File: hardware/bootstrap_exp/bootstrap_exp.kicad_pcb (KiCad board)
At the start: 4 copper layers, 45.7 x 35.6 mm, 32 parts, among them J1 Conn_Coaxial, J2 Conn_Coaxial, U1 OPA810, U2 OPA810, U3 OPA810, U4 OPA810

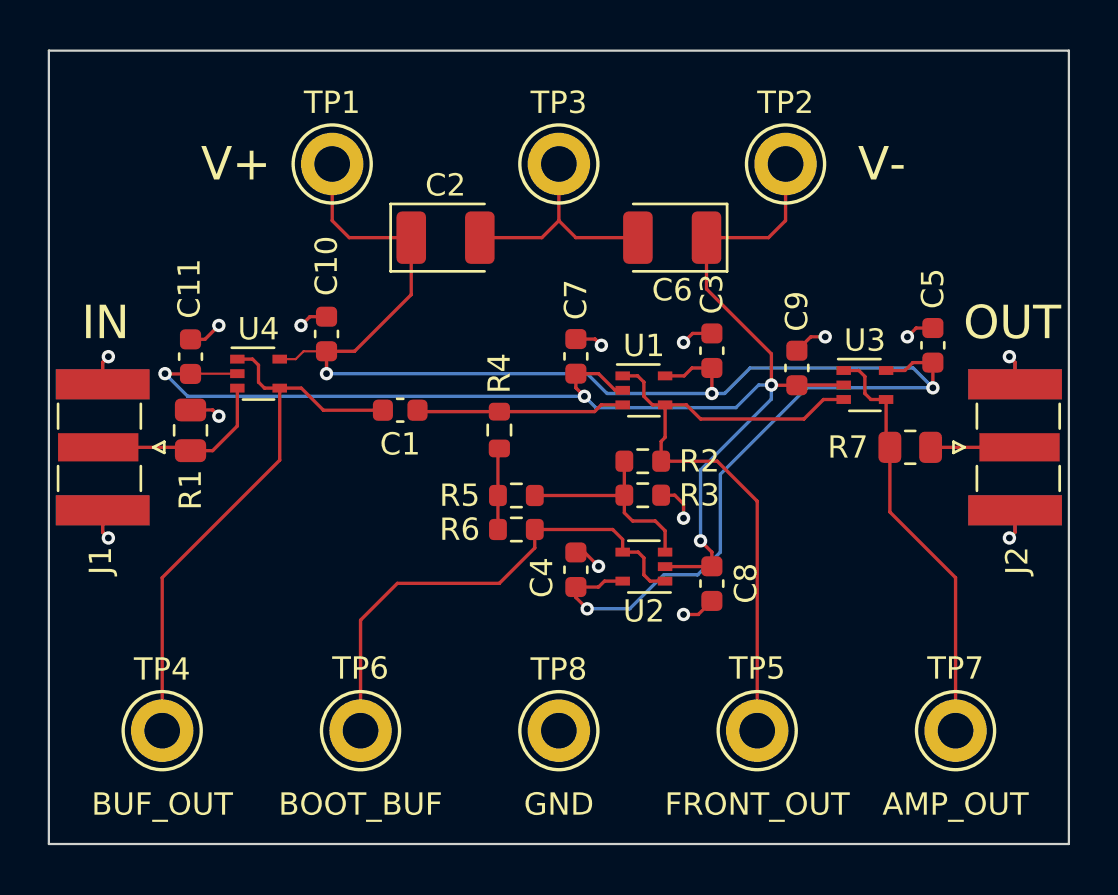
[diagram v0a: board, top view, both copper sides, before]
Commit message: Make edge cut extents an integer for width and height
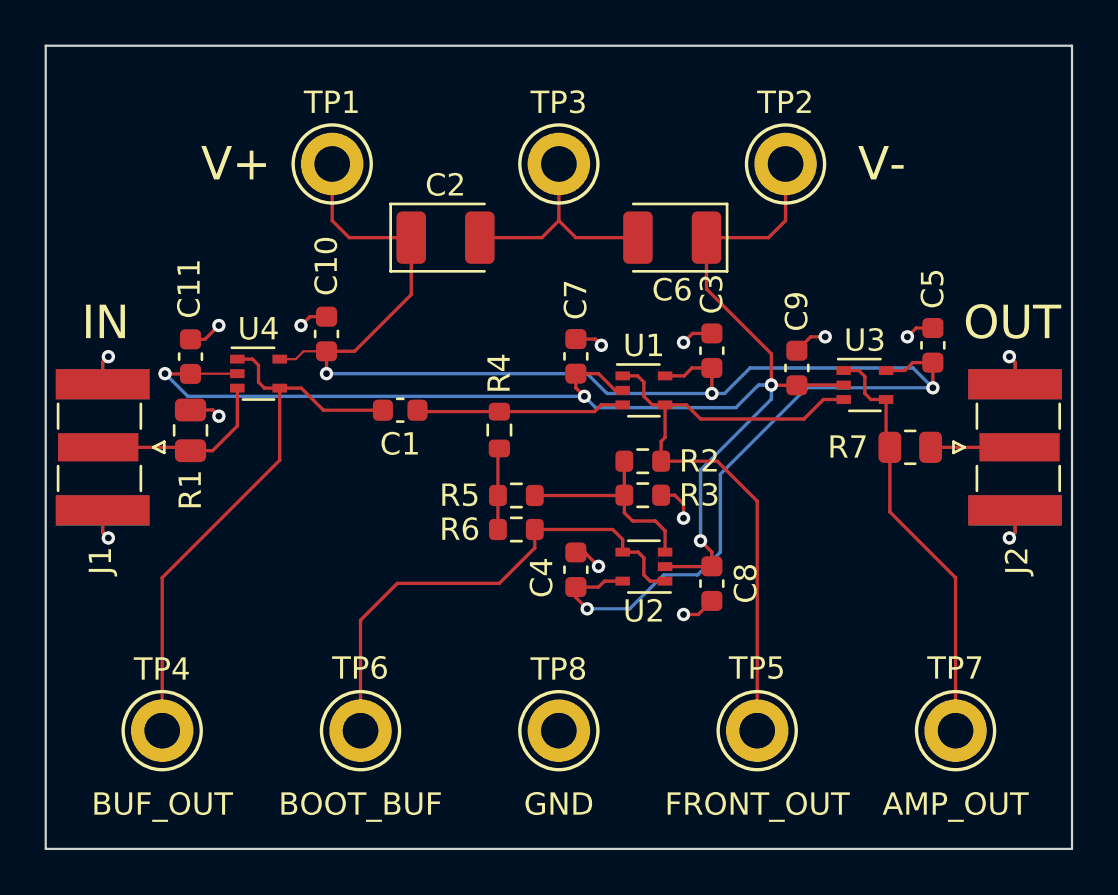
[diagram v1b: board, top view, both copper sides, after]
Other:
- board size 45.7 x 35.6 mm -> 46 x 36 mm
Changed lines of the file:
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@@
       (layerselection 0x00010fc_ffffffff)
       (disableapertmacros false)
-      (usegerberextensions false)
+      (usegerberextensions true)
       (usegerberattributes true)
       (usegerberadvancedattributes true)
-      (creategerberjobfile true)
+      (creategerberjobfile false)
       (svguseinch false)
       (svgprecision 6)
@@
       (plotinvisibletext false)
       (sketchpadsonfab false)
-      (subtractmaskfromsilk false)
+      (subtractmaskfromsilk true)
       (outputformat 1)
       (mirror false)
-      (drillshape 1)
+      (drillshape 0)
       (scaleselection 1)
-      (outputdirectory "")
+      (outputdirectory "output/")
     )
   )
@@
     (fp_line (start -1.75 1.4) (end 1.75 1.4) (layer "F.Fab") (width 0.1))
     (fp_line (start 1.75 1.4) (end 1.75 -1.4) (layer "F.Fab") (width 0.1))
-    (pad "1" smd roundrect (at -1.5375 0) (size 1.325 2.35) (layers "F.Cu" "F.Paste" "F.Mask") (roundrect_rratio 0.188679)
+    (pad "1" smd roundrect (at -1.5375 0) (size 1.325 2.35) (layers "F.Cu" "F.Paste" "F.Mask") (roundrect_rratio 0.1886792453)
       (net 2 "/V+") (pintype "passive"))
-    (pad "2" smd roundrect (at 1.5375 0) (size 1.325 2.35) (layers "F.Cu" "F.Paste" "F.Mask") (roundrect_rratio 0.188679)
+    (pad "2" smd roundrect (at 1.5375 0) (size 1.325 2.35) (layers "F.Cu" "F.Paste" "F.Mask") (roundrect_rratio 0.1886792453)
       (net 3 "GND") (pintype "passive"))
     (model "${KICAD6_3DMODEL_DIR}/Capacitor_Tantalum_SMD.3dshapes/CP_EIA-3528-12_Kemet-T.wrl"
@@
     (fp_line (start 1.75 -1.4) (end -1.05 -1.4) (layer "F.Fab") (width 0.1))
     (fp_line (start -1.75 1.4) (end 1.75 1.4) (layer "F.Fab") (width 0.1))
-    (pad "1" smd roundrect (at -1.5375 0 180) (size 1.325 2.35) (layers "F.Cu" "F.Paste" "F.Mask") (roundrect_rratio 0.188679)
+    (pad "1" smd roundrect (at -1.5375 0 180) (size 1.325 2.35) (layers "F.Cu" "F.Paste" "F.Mask") (roundrect_rratio 0.1886792453)
       (net 4 "/V-") (pintype "passive"))
-    (pad "2" smd roundrect (at 1.5375 0 180) (size 1.325 2.35) (layers "F.Cu" "F.Paste" "F.Mask") (roundrect_rratio 0.188679)
+    (pad "2" smd roundrect (at 1.5375 0 180) (size 1.325 2.35) (layers "F.Cu" "F.Paste" "F.Mask") (roundrect_rratio 0.1886792453)
       (net 3 "GND") (pintype "passive"))
     (model "${KICAD6_3DMODEL_DIR}/Capacitor_Tantalum_SMD.3dshapes/CP_EIA-3528-12_Kemet-T.wrl"
@@
     (fp_line (start -1 0.625) (end -1 -0.625) (layer "F.Fab") (width 0.1))
     (fp_line (start -1 -0.625) (end 1 -0.625) (layer "F.Fab") (width 0.1))
-    (pad "1" smd roundrect (at -0.9125 0 90) (size 1.025 1.4) (layers "F.Cu" "F.Paste" "F.Mask") (roundrect_rratio 0.243902)
+    (pad "1" smd roundrect (at -0.9125 0 90) (size 1.025 1.4) (layers "F.Cu" "F.Paste" "F.Mask") (roundrect_rratio 0.243902439)
       (net 12 "Net-(J1-Pad1)") (pintype "passive"))
-    (pad "2" smd roundrect (at 0.9125 0 90) (size 1.025 1.4) (layers "F.Cu" "F.Paste" "F.Mask") (roundrect_rratio 0.243902)
+    (pad "2" smd roundrect (at 0.9125 0 90) (size 1.025 1.4) (layers "F.Cu" "F.Paste" "F.Mask") (roundrect_rratio 0.243902439)
       (net 3 "GND") (pintype "passive"))
     (model "${KICAD6_3DMODEL_DIR}/Resistor_SMD.3dshapes/R_0805_2012Metric.wrl"
@@
     (fp_line (start 1 -0.625) (end 1 0.625) (layer "F.Fab") (width 0.1))
     (fp_line (start 1 0.625) (end -1 0.625) (layer "F.Fab") (width 0.1))
-    (pad "1" smd roundrect (at -0.9125 0) (size 1.025 1.4) (layers "F.Cu" "F.Paste" "F.Mask") (roundrect_rratio 0.243902)
+    (pad "1" smd roundrect (at -0.9125 0) (size 1.025 1.4) (layers "F.Cu" "F.Paste" "F.Mask") (roundrect_rratio 0.243902439)
       (net 11 "/AMP_OUT") (pintype "passive"))
-    (pad "2" smd roundrect (at 0.9125 0) (size 1.025 1.4) (layers "F.Cu" "F.Paste" "F.Mask") (roundrect_rratio 0.243902)
+    (pad "2" smd roundrect (at 0.9125 0) (size 1.025 1.4) (layers "F.Cu" "F.Paste" "F.Mask") (roundrect_rratio 0.243902439)
       (net 6 "Net-(J2-Pad1)") (pintype "passive"))
     (model "${KICAD6_3DMODEL_DIR}/Resistor_SMD.3dshapes/R_0805_2012Metric.wrl"
@@
     )
   )
-  (gr_rect (start 111.76 78.74) (end 157.48 114.3) (layer "Edge.Cuts") (width 0.1) (fill none))
+  (gr_rect (start 111.62 78.52) (end 157.62 114.52) (layer "Edge.Cuts") (width 0.1) (fill none))
   (gr_text "GND" (at 134.62 112.522) (layer "F.SilkS")
     (effects (font (size 1 1) (thickness 0.15)))
@@
     (polygon
       (pts
-        (xy 157.734 114.554)
-        (xy 111.506 114.554)
-        (xy 111.506 78.486)
-        (xy 157.734 78.486)
+        (xy 157.861 114.681)
+        (xy 111.379 114.681)
+        (xy 111.379 78.359)
+        (xy 157.861 78.359)
       )
     )

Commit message: Nudge connectors closer to new edge
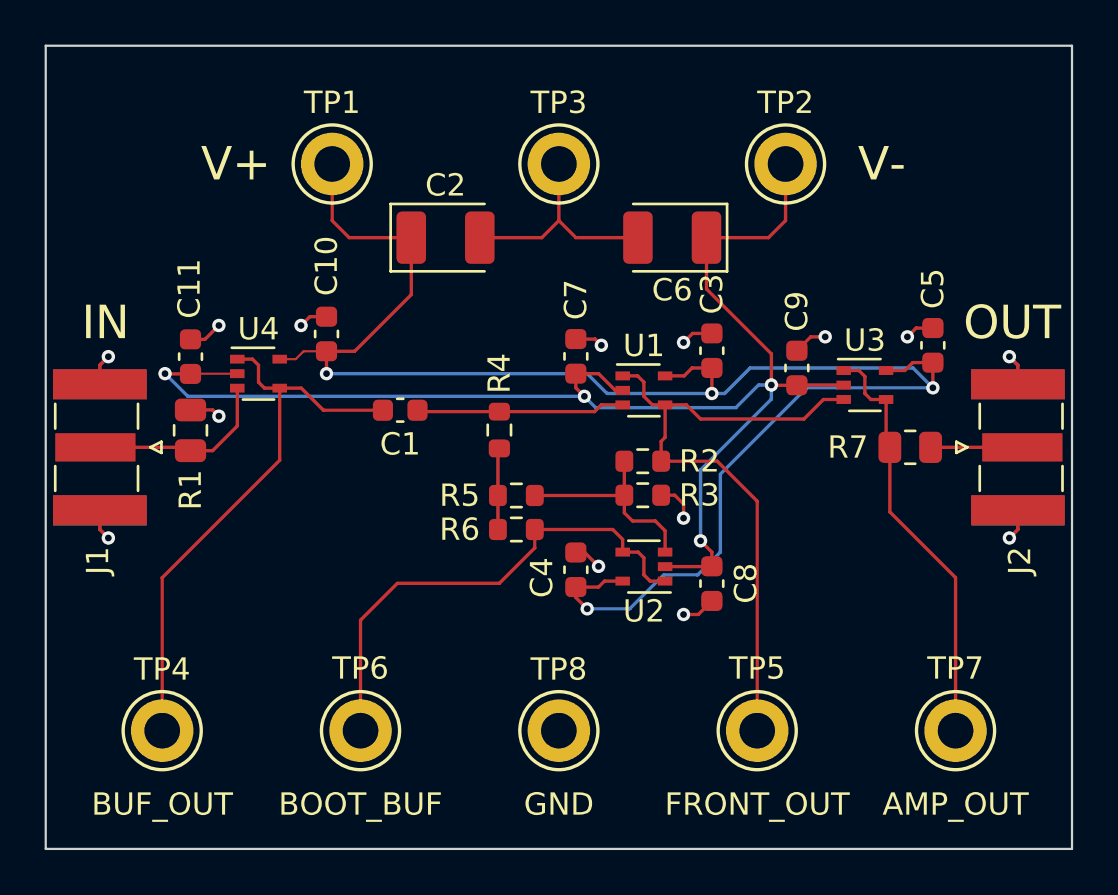
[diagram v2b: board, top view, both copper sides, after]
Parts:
- moved J1 0.13 mm to (114.0, 96.5)
- moved J2 0.13 mm to (155.2, 96.5)
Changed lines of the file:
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@@
   )
   (footprint "Connector_Coaxial:SMA_Samtec_SMA-J-P-X-ST-EM1_EdgeMount" (layer "F.Cu")
-    (at 155.067 96.52 90)
+    (at 155.194 96.52 90)
     (descr "Connector SMA, 0Hz to 20GHz, 50Ohm, Edge Mount (http://suddendocs.samtec.com/prints/sma-j-p-x-st-em1-mkt.pdf)")
     (tags "SMA Straight Samtec Edge Mount")
@@
   )
   (footprint "Connector_Coaxial:SMA_Samtec_SMA-J-P-X-ST-EM1_EdgeMount" (layer "F.Cu")
-    (at 114.173 96.52 -90)
+    (at 114.046 96.52 -90)
     (descr "Connector SMA, 0Hz to 20GHz, 50Ohm, Edge Mount (http://suddendocs.samtec.com/prints/sma-j-p-x-st-em1-mkt.pdf)")
     (tags "SMA Straight Samtec Edge Mount")
@@
   (segment (start 141.859 101.219) (end 141.859 97.7265) (width 0.15) (layer "B.Cu") (net 2))
   (segment (start 141.478 103.404) (end 140.869 104.013) (width 0.15) (layer "F.Cu") (net 3))
-  (segment (start 114.173 100.33) (end 114.427 100.584) (width 0.15) (layer "F.Cu") (net 3))
+  (segment (start 114.046 92.837) (end 114.427 92.456) (width 0.15) (layer "F.Cu") (net 3))
   (segment (start 150.635 91.173) (end 150.241 91.567) (width 0.15) (layer "F.Cu") (net 3))
   (segment (start 118.11 94.8455) (end 119.1025 94.8455) (width 0.15) (layer "F.Cu") (net 3))
-  (segment (start 114.173 93.695) (end 114.173 92.71) (width 0.15) (layer "F.Cu") (net 3))
-  (segment (start 155.067 100.33) (end 154.813 100.584) (width 0.15) (layer "F.Cu") (net 3))
   (segment (start 140.208 99.695) (end 140.208 99.06) (width 0.15) (layer "F.Cu") (net 3))
   (segment (start 141.478 91.414) (end 140.615 91.414) (width 0.15) (layer "F.Cu") (net 3))
-  (segment (start 114.173 99.345) (end 114.173 100.33) (width 0.15) (layer "F.Cu") (net 3))
+  (segment (start 154.813 100.584) (end 155.194 100.203) (width 0.15) (layer "F.Cu") (net 3))
   (segment (start 135.382 87.122) (end 138.1625 87.122) (width 0.15) (layer "F.Cu") (net 3))
   (segment (start 131.0775 87.122) (end 133.858 87.122) (width 0.15) (layer "F.Cu") (net 3))
-  (segment (start 155.067 93.695) (end 155.067 92.71) (width 0.15) (layer "F.Cu") (net 3))
+  (segment (start 155.194 92.837) (end 155.194 93.695) (width 0.15) (layer "F.Cu") (net 3))
   (segment (start 151.384 91.173) (end 150.635 91.173) (width 0.15) (layer "F.Cu") (net 3))
   (segment (start 135.382 91.668) (end 136.245 91.668) (width 0.15) (layer "F.Cu") (net 3))
@@
   (segment (start 118.11 91.681) (end 118.758 91.681) (width 0.15) (layer "F.Cu") (net 3))
   (segment (start 119.1025 94.8455) (end 119.38 95.123) (width 0.15) (layer "F.Cu") (net 3))
-  (segment (start 114.173 92.71) (end 114.427 92.456) (width 0.15) (layer "F.Cu") (net 3))
   (segment (start 134.62 86.36) (end 134.62 83.82) (width 0.15) (layer "F.Cu") (net 3))
   (segment (start 140.615 91.414) (end 140.208 91.821) (width 0.15) (layer "F.Cu") (net 3))
+  (segment (start 155.194 100.203) (end 155.194 99.345) (width 0.15) (layer "F.Cu") (net 3))
   (segment (start 118.758 91.681) (end 119.38 91.059) (width 0.15) (layer "F.Cu") (net 3))
   (segment (start 123.063 91.059) (end 123.457 90.665) (width 0.15) (layer "F.Cu") (net 3))
   (segment (start 134.62 86.36) (end 135.382 87.122) (width 0.15) (layer "F.Cu") (net 3))
-  (segment (start 155.067 92.71) (end 154.813 92.456) (width 0.15) (layer "F.Cu") (net 3))
+  (segment (start 114.046 93.695) (end 114.046 92.837) (width 0.15) (layer "F.Cu") (net 3))
   (segment (start 145.288 92.189) (end 145.91 91.567) (width 0.15) (layer "F.Cu") (net 3))
   (segment (start 133.858 87.122) (end 134.62 86.36) (width 0.15) (layer "F.Cu") (net 3))
+  (segment (start 154.813 92.456) (end 155.194 92.837) (width 0.15) (layer "F.Cu") (net 3))
   (segment (start 140.208 99.06) (end 139.814 98.666) (width 0.15) (layer "F.Cu") (net 3))
   (segment (start 136.245 91.668) (end 136.525 91.948) (width 0.15) (layer "F.Cu") (net 3))
   (segment (start 145.91 91.567) (end 146.558 91.567) (width 0.15) (layer "F.Cu") (net 3))
-  (segment (start 155.067 99.345) (end 155.067 100.33) (width 0.15) (layer "F.Cu") (net 3))
   (segment (start 140.869 104.013) (end 140.208 104.013) (width 0.15) (layer "F.Cu") (net 3))
+  (segment (start 114.046 99.345) (end 114.046 100.203) (width 0.15) (layer "F.Cu") (net 3))
   (segment (start 135.776 101.232) (end 136.398 101.854) (width 0.15) (layer "F.Cu") (net 3))
   (segment (start 123.457 90.665) (end 124.206 90.665) (width 0.15) (layer "F.Cu") (net 3))
+  (segment (start 114.046 100.203) (end 114.427 100.584) (width 0.15) (layer "F.Cu") (net 3))
   (segment (start 139.814 98.666) (end 139.2042 98.666) (width 0.15) (layer "F.Cu") (net 3))
   (via (at 154.813 100.584) (size 0.6) (drill 0.3) (layers "F.Cu" "B.Cu") (net 3))
@@
   (via (at 136.525 91.948) (size 0.6) (drill 0.3) (layers "F.Cu" "B.Cu") (net 3))
   (via (at 114.427 100.584) (size 0.6) (drill 0.3) (layers "F.Cu" "B.Cu") (net 3))
-  (segment (start 114.173 92.71) (end 114.427 92.456) (width 0.15) (layer "B.Cu") (net 3))
-  (segment (start 114.173 100.33) (end 114.427 100.584) (width 0.15) (layer "B.Cu") (net 3))
-  (segment (start 155.067 100.33) (end 154.813 100.584) (width 0.15) (layer "B.Cu") (net 3))
-  (segment (start 155.067 92.71) (end 154.813 92.456) (width 0.15) (layer "B.Cu") (net 3))
-  (segment (start 155.067 93.695) (end 155.067 92.71) (width 0.15) (layer "B.Cu") (net 3))
-  (segment (start 155.067 99.345) (end 155.067 100.33) (width 0.15) (layer "B.Cu") (net 3))
-  (segment (start 114.173 93.695) (end 114.173 92.71) (width 0.15) (layer "B.Cu") (net 3))
-  (segment (start 114.173 99.345) (end 114.173 100.33) (width 0.15) (layer "B.Cu") (net 3))
+  (segment (start 114.046 100.203) (end 114.427 100.584) (width 0.15) (layer "B.Cu") (net 3))
+  (segment (start 114.046 99.345) (end 114.046 100.203) (width 0.15) (layer "B.Cu") (net 3))
+  (segment (start 154.813 92.456) (end 155.194 92.837) (width 0.15) (layer "B.Cu") (net 3))
+  (segment (start 154.813 100.584) (end 155.194 100.203) (width 0.15) (layer "B.Cu") (net 3))
+  (segment (start 114.046 93.695) (end 114.046 92.837) (width 0.15) (layer "B.Cu") (net 3))
+  (segment (start 155.194 100.203) (end 155.194 99.345) (width 0.15) (layer "B.Cu") (net 3))
+  (segment (start 155.194 92.837) (end 155.194 93.695) (width 0.15) (layer "B.Cu") (net 3))
+  (segment (start 114.046 92.837) (end 114.427 92.456) (width 0.15) (layer "B.Cu") (net 3))
   (segment (start 144.78 86.36) (end 144.018 87.122) (width 0.15) (layer "F.Cu") (net 4))
   (segment (start 136.398 93.218) (end 135.382 93.218) (width 0.15) (layer "F.Cu") (net 4))
@@
   (segment (start 128.347 94.92) (end 131.953 94.92) (width 0.15) (layer "F.Cu") (net 5))
   (segment (start 131.953 94.92) (end 136.22 94.92) (width 0.15) (layer "F.Cu") (net 5))
-  (segment (start 151.2805 96.52) (end 155.267 96.52) (width 0.15) (layer "F.Cu") (net 6))
+  (segment (start 151.2805 96.52) (end 155.394 96.52) (width 0.15) (layer "F.Cu") (net 6))
   (segment (start 140.337 94.617) (end 140.97 95.25) (width 0.15) (layer "F.Cu") (net 7))
   (segment (start 145.6055 95.25) (end 146.4795 94.376) (width 0.15) (layer "F.Cu") (net 7))
@@
   (segment (start 147.386 93.076) (end 148.067 93.076) (width 0.15) (layer "F.Cu") (net 11))
   (segment (start 117.9595 96.52) (end 118.11 96.6705) (width 0.15) (layer "F.Cu") (net 12))
+  (segment (start 113.846 96.52) (end 117.9595 96.52) (width 0.15) (layer "F.Cu") (net 12))
   (segment (start 120.208 93.868) (end 120.208 95.565) (width 0.15) (layer "F.Cu") (net 12))
   (segment (start 120.208 95.565) (end 119.1025 96.6705) (width 0.15) (layer "F.Cu") (net 12))
-  (segment (start 113.973 96.52) (end 117.9595 96.52) (width 0.15) (layer "F.Cu") (net 12))
   (segment (start 119.1025 96.6705) (end 118.11 96.6705) (width 0.15) (layer "F.Cu") (net 12))
   (zone (net 3) (net_name "GND") (layers "In1.Cu" "In2.Cu") (hatch edge 0.508)
